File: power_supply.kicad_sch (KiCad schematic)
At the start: 57 parts, among them Q4 Q_FDC6561AN, SW9 1825232-1, U1 INA219BIDR, U2 MIC2250-1YD5-TR, U3 MCP73871T-2CCI/ML, U5 AP9101CAK6-ABTRG1

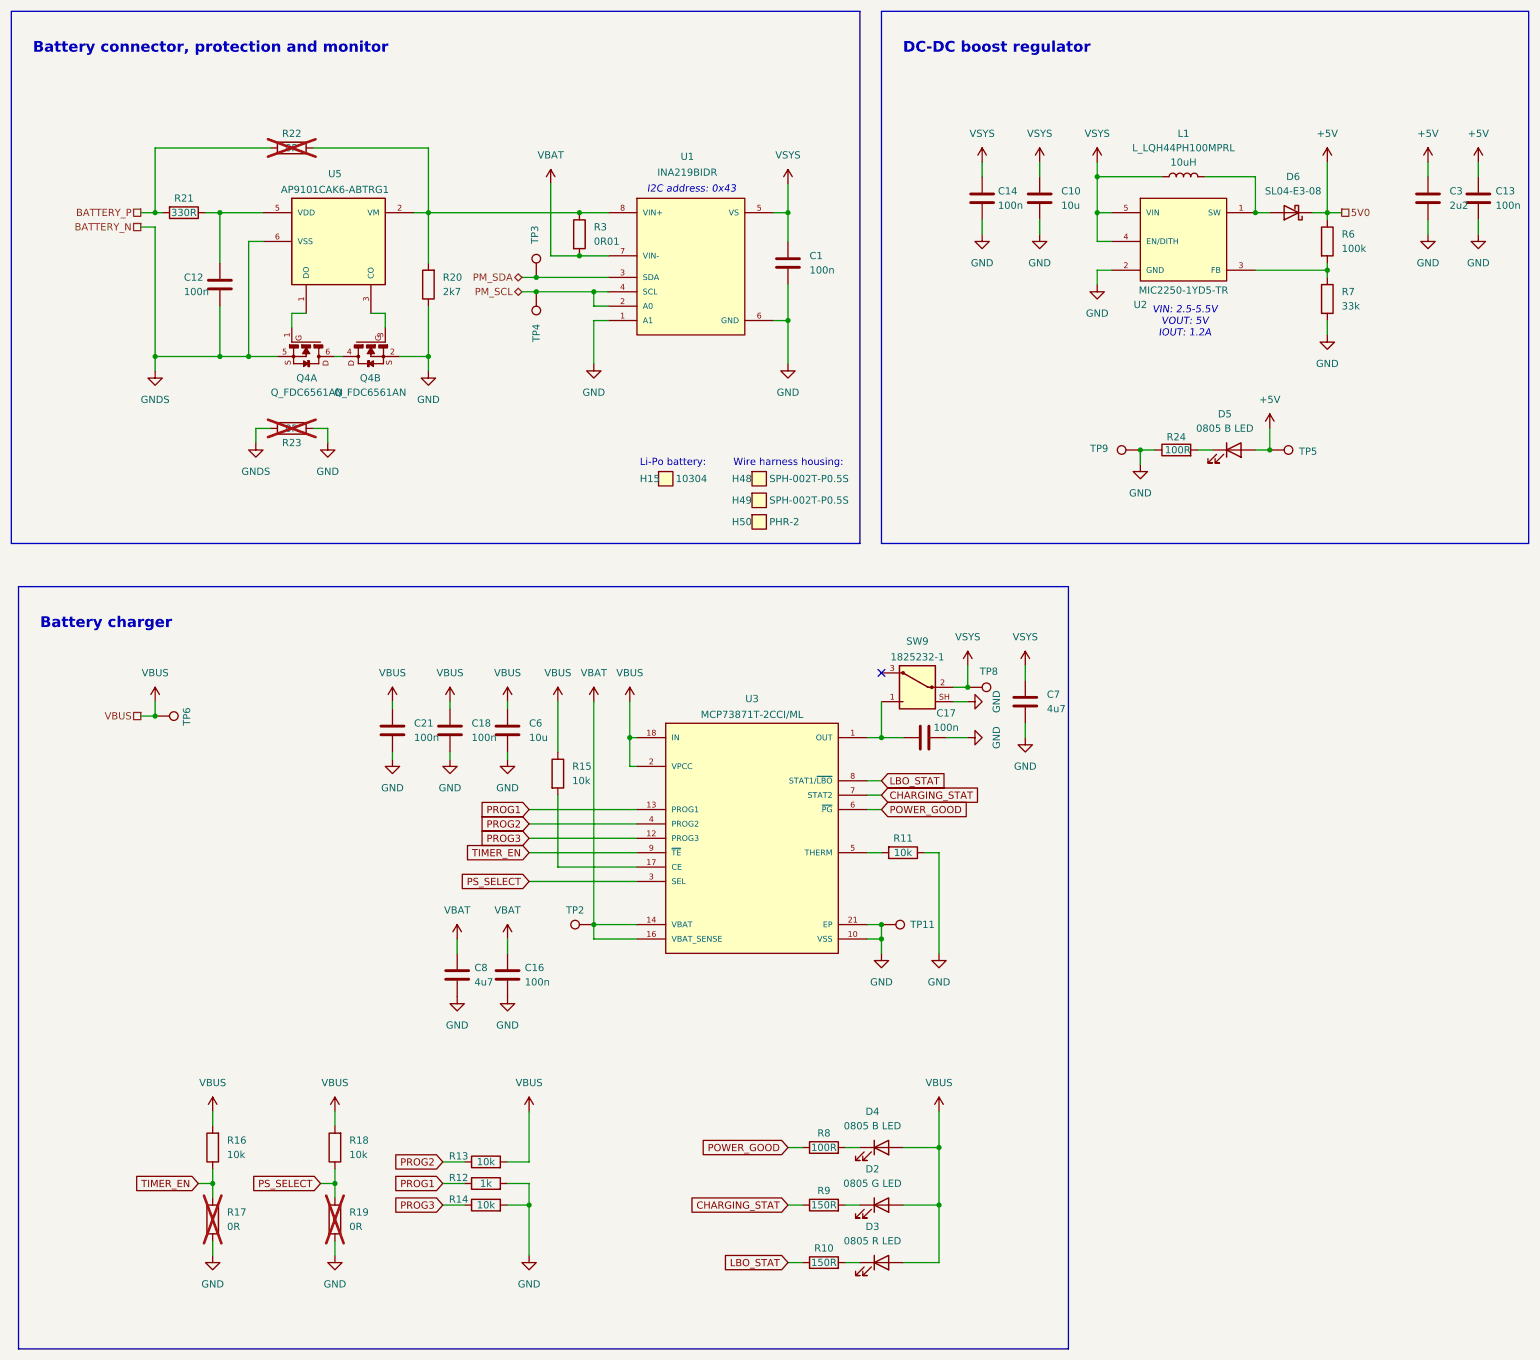
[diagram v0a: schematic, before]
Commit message: Fixes to power charger, cleanup schematic
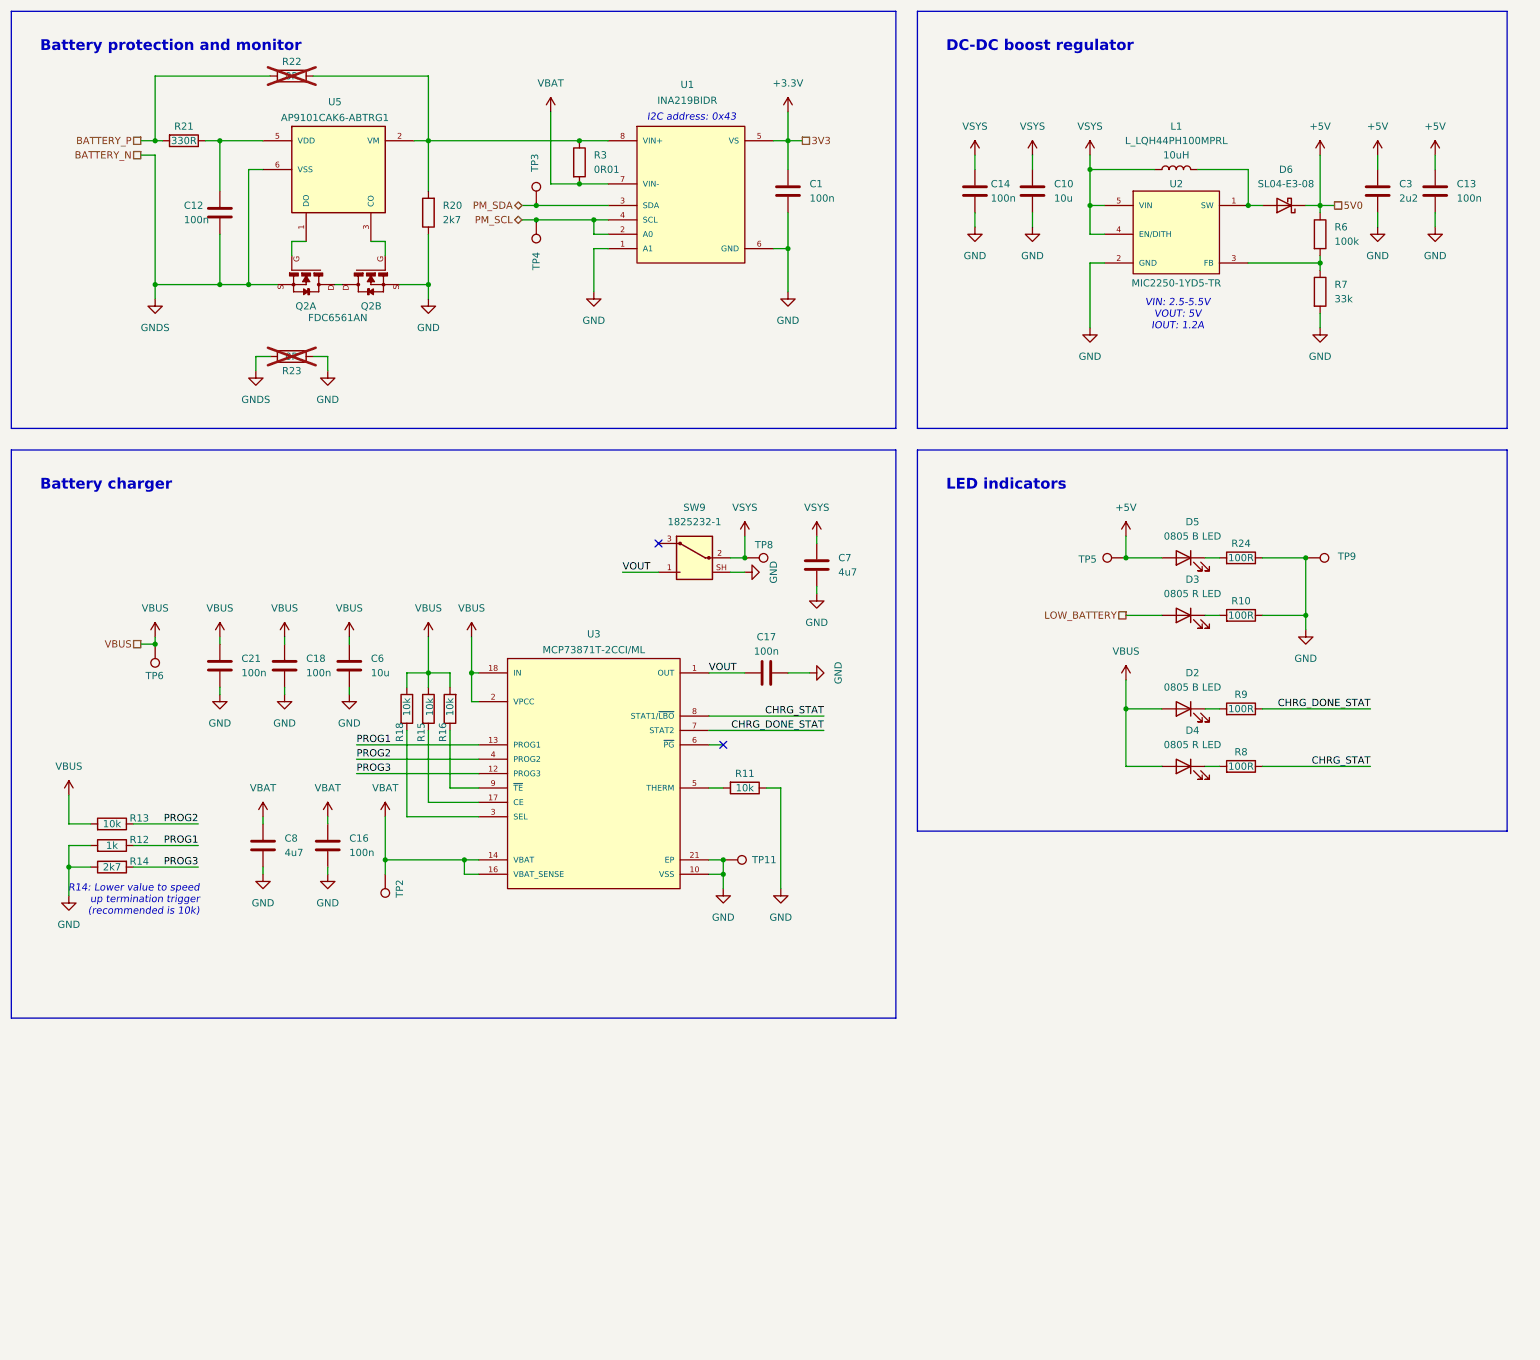
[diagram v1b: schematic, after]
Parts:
- removed D2: 0805 G LED, library:LED_0805_2012Metric, symbol library:LED_G_MP008291
- removed D4: 0805 B LED, library:LED_0805_2012Metric, symbol library:LED_B_MP008292
- removed H15: 10304, library:Li-Pol_battery_8x30x40mm, symbol library:10304
- removed H48, H49: SPH-002T-P0.5S, symbol library:SPH-002T-P0.5S
- removed H50: PHR-2, symbol library:PHR-2
- removed Q4: Q_FDC6561AN, library:SSOT-6, symbol library:Q_FDC6561AN
- removed R10, R9: 150R, library:R_0402_1005Metric, symbol library:R_150R_0402
- removed R14: 10k, library:R_0402_1005Metric, symbol library:R_10k_0402
- removed R17, R19: 0R, library:R_0402_1005Metric, symbol library:R_0R_0402
- added D2: 0805 B LED, library:LED_0805_2012Metric, symbol library:LED_B_MP008292
- added D4: 0805 R LED, library:LED_0805_2012Metric, symbol library:LED_R_MP008293
- added Q2: Q_FDC6561AN, library:SSOT-6, symbol library:Q_FDC6561AN
- added R10, R9: 100R, library:R_0402_1005Metric, symbol library:R_100R_0402
- added R14: 2k7, library:R_0402_1005Metric, symbol library:R_2k7_0402
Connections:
- net GND: now also Q2.2, R10.1, R14.1
- net GNDS: now also Q2.5
- net PROG3: now also R14.2
- net VBUS: now also R18.1, D2.2 (A), D4.2 (A); no longer D3.2 (A), R18.2
- net VSYS: no longer C1.1, U1.5 (VS)
- net at U5.3 (CO): now also Q2.3
- net VOUT: now reaches C17.2, SW9.1, U3.1 (OUT), U3.20 (OUT)
- net at D3.1 (K): now also R10.2
- net at U5.1 (DO): now also Q2.1
- net at R8.2: now also D4.1 (K)
- net CHARGING_STAT renamed CHRG_DONE_STAT
- net CHRG_DONE_STAT: now also R9.1
- net LBO_STAT renamed CHRG_STAT
- net CHRG_STAT: now also R8.1
- net POWER_GOOD: no longer names the net of U3.6 (~{PG})
- net POWER_GOOD: no longer R8.1
- net PS_SELECT: no longer names the net of U3.3 (SEL)
- net PS_SELECT: now also R18.2; no longer R18.1
- net TIMER_EN: no longer names the net of R16.1, U3.9 (~{TE})
- new net: Q2.4, Q2.6
- new net: D2.1 (K), R9.2
- new net +3.3V: C1.1, U1.5 (VS)
- new net LOW_BATTERY: D3.2 (A)
- no-connect marks 1 -> 2
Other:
- note added: "Battery protection and monitor"
- note added: "LED indicators"
- note added: "R14: Lower value to speed up termination trigger (recommended is 10k)"
- note removed: "Battery connector, protection and monitor"
- note removed: "Li-Po battery:"
- note removed: "Wire harness housing:"
- title: (none) -> SnapHAT
- moved on the sheet: C1, C10, C12, C13, C14, C16, C17, C18, C21, C3, C6, C7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

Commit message: Start updating PCB, library fixes
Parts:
- R10: value 100R -> 47R; symbol library:R_100R_0402 -> library:R_47R_0402; Part number RC0402JR-07100RL -> RC0402JR-0747RL
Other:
- moved on the sheet: C10, C13, C14, C3

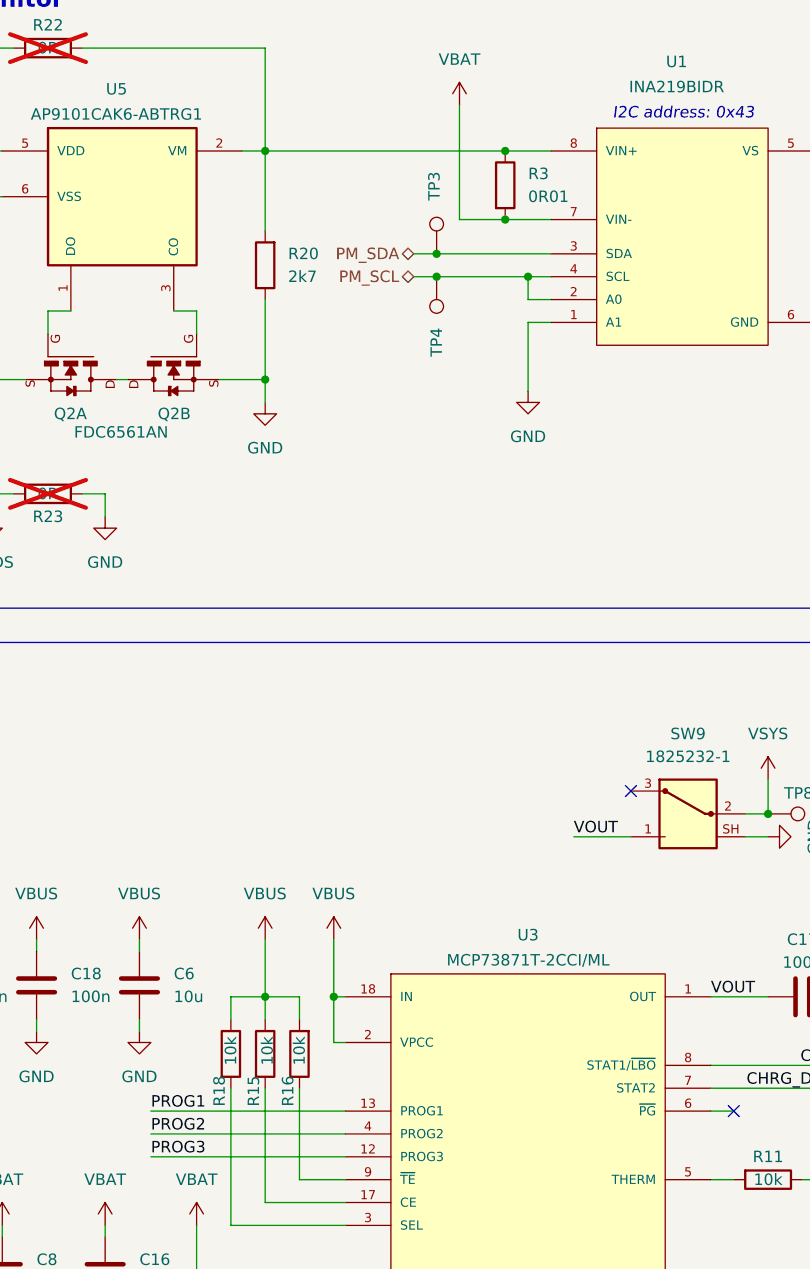
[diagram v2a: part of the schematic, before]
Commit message: Arrange designators, clear DRC, cleanups
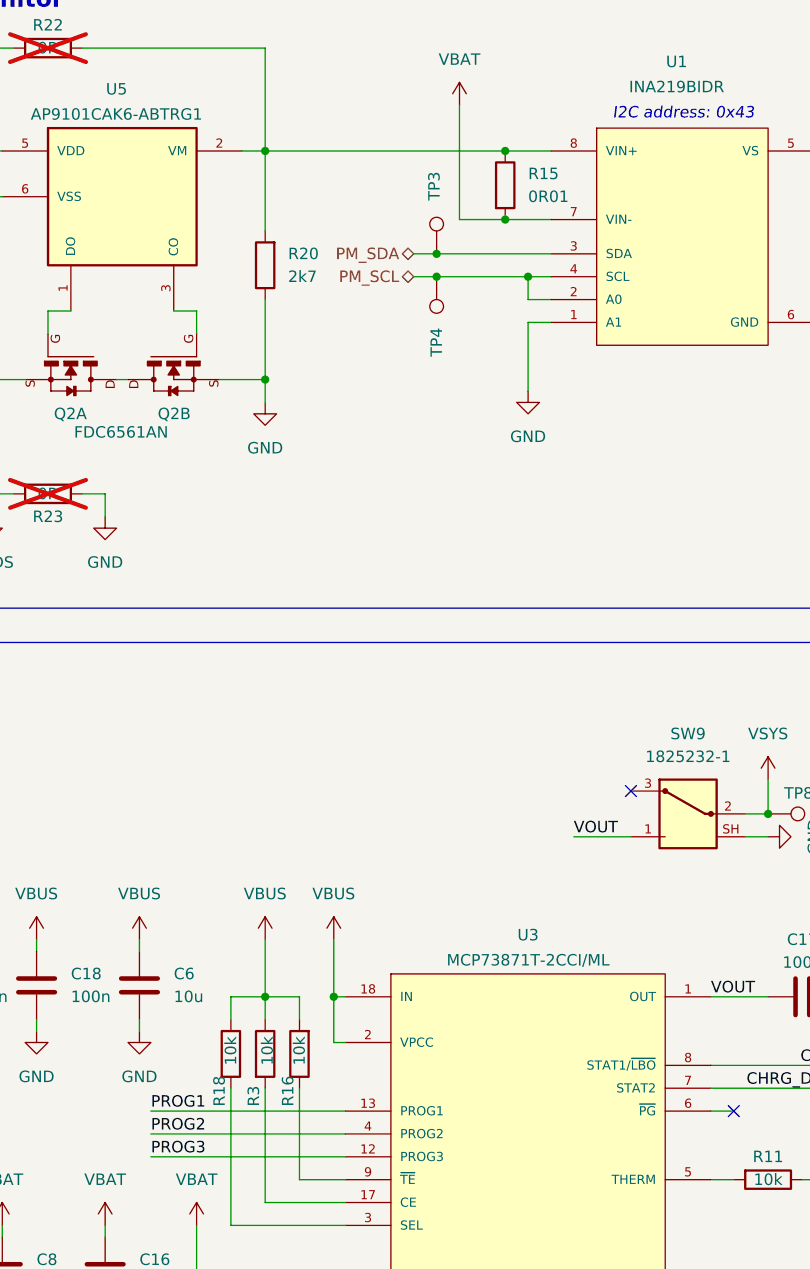
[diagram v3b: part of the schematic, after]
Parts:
- renumbered R3 to R15, R15 to R3
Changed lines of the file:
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@@
 		(dnp no)
 		(fields_autoplaced yes)
-		(property "Reference" "R3"
+		(property "Reference" "R15"
 			(at 119.38 41.9099 0)
 			(effects
@@
 			(project "snaphat"
 				(path "/1b9269fa-3ac8-429a-ab83-4cc9a4203d51/51746a52-7f52-4ac2-bd2d-8efe72ed4090"
-					(reference "R3")
+					(reference "R15")
 					(unit 1)
 				)
@@
 		(on_board yes)
 		(dnp no)
-		(property "Reference" "R15"
+		(property "Reference" "R3"
 			(at 88.9 145.542 90)
 			(effects
@@
 			(project "snaphat"
 				(path "/1b9269fa-3ac8-429a-ab83-4cc9a4203d51/51746a52-7f52-4ac2-bd2d-8efe72ed4090"
-					(reference "R15")
+					(reference "R3")
 					(unit 1)
 				)
@@
 			(effects
 				(font
+					(face "Quicksand")
 					(size 1.27 1.27)
 				)
@@
 			(effects
 				(font
+					(face "Quicksand")
 					(size 1.27 1.27)
 				)
@@
 			(effects
 				(font
+					(face "Quicksand")
 					(size 1.27 1.27)
 				)
@@
 			(effects
 				(font
+					(face "Quicksand")
 					(size 1.27 1.27)
 				)
@@
 			(effects
 				(font
+					(face "Quicksand")
 					(size 1.27 1.27)
 				)
@@
 			(effects
 				(font
+					(face "Quicksand")
 					(size 1.27 1.27)
 				)

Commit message: Fixes to library, add updated schematic PDF and BOM
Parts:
- D6: Manufacturer (none) -> Vishay; Part number (none) -> SL04-E3-08
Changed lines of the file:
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@@
+			)
+		)
+		(property "Part number" "SL04-E3-08"
+			(at 241.3 50.8 0)
+			(effects
+				(font
+					(size 1.27 1.27)
+				)
+				(hide yes)
+			)
+		)
+		(property "Manufacturer" "Vishay"
+			(at 241.3 50.8 0)
+			(effects
+				(font
+					(size 1.27 1.27)
+				)
+				(hide yes)
 			)
 		)

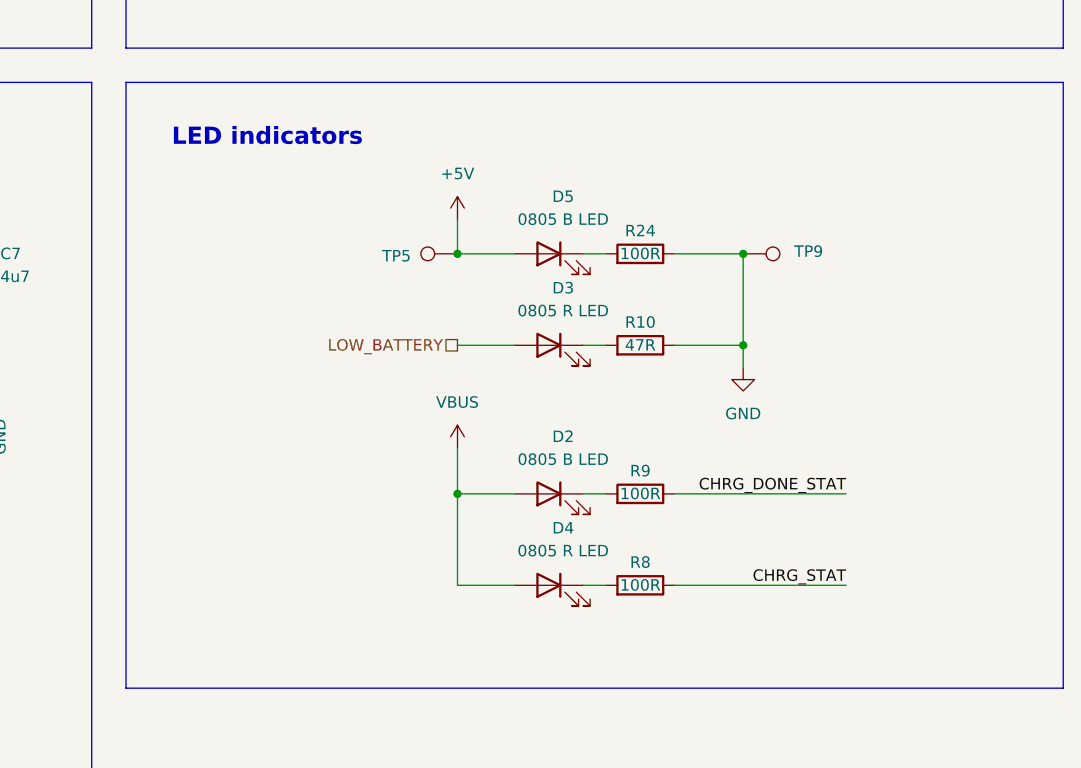
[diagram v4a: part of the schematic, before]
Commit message: Add LED_SHUTTER
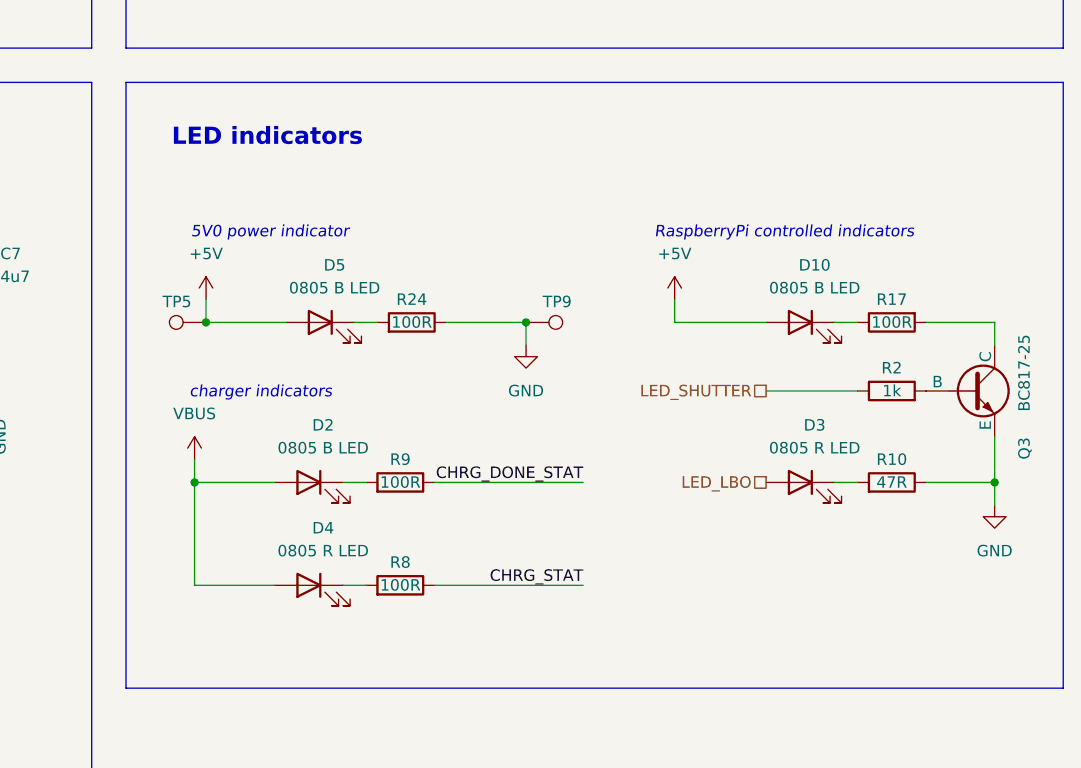
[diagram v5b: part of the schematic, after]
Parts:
- added D10: 0805 B LED, library:LED_0805_2012Metric, symbol library:LED_B_MP008292
- added Q3: Q_BC817-25, library:SOT-23, symbol library:Q_BC817-25
- added R17: 100R, library:R_0402_1005Metric, symbol library:R_100R_0402
- added R2: 1k, library:R_0402_1005Metric, symbol library:R_1k_0402
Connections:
- net +5V: now also D10.2 (A)
- net GND: now also Q3.2 (E)
- net LOW_BATTERY renamed LED_LBO
- new net: D10.1 (K), R17.1
- new net: Q3.3 (C), R17.2
- new net: Q3.1 (B), R2.2
- new net LED_SHUTTER: R2.1
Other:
- note added: "5V0 power indicator"
- note added: "RaspberryPi controlled indicators"
- note added: "charger indicators"
- moved on the sheet: D2, D3, D4, D5, R10, R24, R8, R9, TP5, TP9
